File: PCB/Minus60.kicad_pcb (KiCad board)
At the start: 2 copper layers, 285.2 x 77.2 mm, 79 parts, among them P0 USB, SW0 SW_PUSH, SW0:0 SWITCH_DIODE, SW0:1 SWITCH_DIODE, SW0:10 SWITCH_DIODE, SW0:11 SWITCH_DIODE, SW0:12 SWITCH_DIODE, SW0:13 SWITCH_DIODE, SW0:2 SWITCH_DIODE, SW0:3 SWITCH_DIODE, SW0:4 SWITCH_DIODE, SW0:5 SWITCH_DIODE, SW0:6 SWITCH_DIODE, SW0:7 SWITCH_DIODE, SW0:8 SWITCH_DIODE, SW0:9 SWITCH_DIODE, SW1:0 SWITCH_DIODE, SW1:1 SWITCH_DIODE, SW1:10 SWITCH_DIODE, SW1:11 SWITCH_DIODE, SW1:13 SWITCH_DIODE, SW1:2 SWITCH_DIODE, SW1:3 SWITCH_DIODE, SW1:4 SWITCH_DIODE, SW1:5 SWITCH_DIODE, SW1:6 SWITCH_DIODE, SW1:7 SWITCH_DIODE, SW1:8 SWITCH_DIODE, SW1:9 SWITCH_DIODE, SW2:0 SWITCH_DIODE, SW2:10 SWITCH_DIODE, SW2:11 SWITCH_DIODE, SW2:13 SWITCH_DIODE, SW2:2 SWITCH_DIODE, SW2:3 SWITCH_DIODE, SW2:4 SWITCH_DIODE, SW2:5 SWITCH_DIODE, SW2:6 SWITCH_DIODE, SW2:7 SWITCH_DIODE, SW2:8 SWITCH_DIODE, SW2:9 SWITCH_DIODE, SW3:0 SWITCH_DIODE, SW3:1 SWITCH_DIODE, SW3:10 SWITCH_DIODE, SW3:11 SWITCH_DIODE, SW3:12 SWITCH_DIODE, SW3:13 SWITCH_DIODE, SW3:3 SWITCH_DIODE, SW3:6 SWITCH_DIODE

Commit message: Add stabilizers
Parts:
- added ?: , Keyboards:VIA-0.6, F.Cu at (138.2, 94.0)
- UW0: value USBWireConnection -> (none)
- moved ? 90.3 mm to (266.2, 33.0)
- moved ? 44.4 mm to (180.1, 89.4)
- moved ? 41.2 mm to (120.1, 91.7)
- moved PM0 15.8 mm to (168.1, 93.0)
- moved ? 14.7 mm to (136.9, 101.6)
- moved ? 14.3 mm to (149.9, 100.1)
- moved ? 12.3 mm to (161.0, 73.7)
- moved SW0 8.87 mm to (98.6, 98.6), turned to 180 degrees
- moved ? 3.18 mm to (144.8, 87.1)
- moved UW0 1.61 mm to (148.3, 86.4), turned to 45 degrees
- moved ? 1.27 mm to (137.2, 93.5), turned to 0 degrees
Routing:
- net /COL13: track 155.3 -> 181.4 mm, vias 1 -> 0
- net /COL9: track 68.1 -> 88.5 mm
- net /COL12: track 127.6 -> 144.4 mm
- net /COL6: track 136.0 -> 119.2 mm
- net /COL10: track 112.0 -> 127.6 mm, vias 0 -> 1
- net /COL4: track 162.8 -> 147.8 mm
- net /COL11: track 120.8 -> 135.2 mm
- net /COL7: track 83.3 -> 70.0 mm, vias 2 -> 0
- net /COL3: track 199.6 -> 186.8 mm, vias 1 -> 2
- net /COL5: track 143.5 -> 131.5 mm, vias 2 -> 0
- net /COL1: track 216.0 -> 204.1 mm, vias 3 -> 1
- net /RST: track 81.3 -> 71.1 mm
- net /COL0: track 234.3 -> 226.4 mm, vias 3 -> 1
- net /ROW3: track 286.2 -> 289.7 mm
- net /COL2: track 194.7 -> 197.0 mm, vias 3 -> 2
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
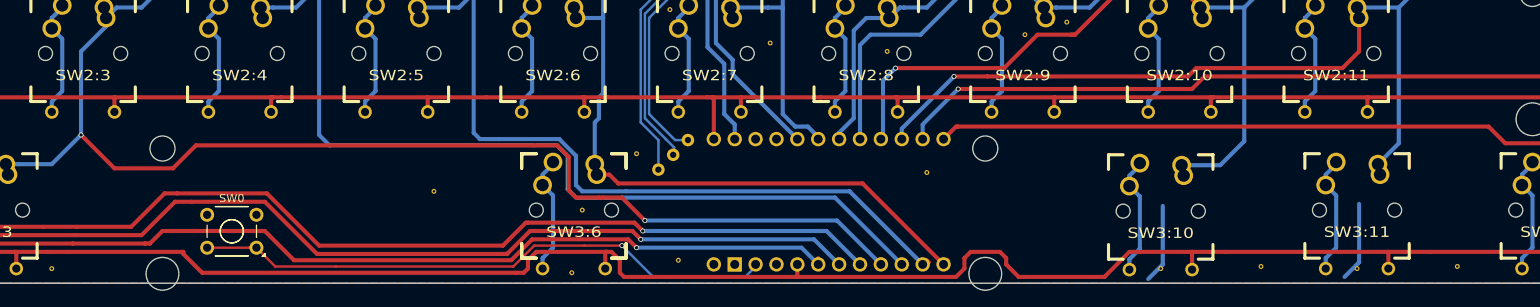
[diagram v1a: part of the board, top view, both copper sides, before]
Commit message: Flip spacebar stabilizer
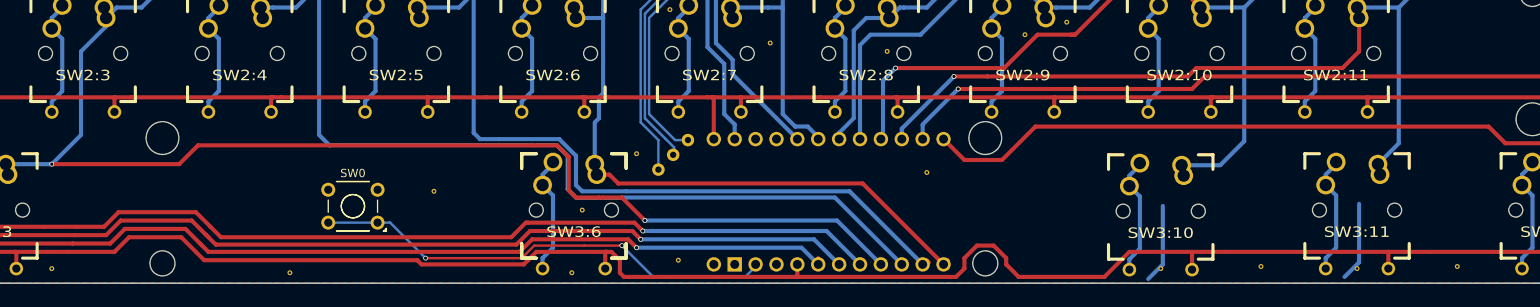
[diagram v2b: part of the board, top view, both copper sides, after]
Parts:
- added ?: , Keyboards:VIA-0.6, F.Cu at (102.6, 101.6)
- moved SW0 15.0 mm to (113.3, 95.5)
- turned ? to 180 degrees
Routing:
- net /RST: track 71.1 -> 56.8 mm, vias 1 -> 2
- net /COL1: track 204.1 -> 201.2 mm
- net /COL2: track 197.0 -> 194.3 mm
- net /COL13: track 181.4 -> 183.5 mm
- net /COL3: track 186.8 -> 188.4 mm
- net /COL0: track 226.4 -> 225.8 mm
- net /ROW3: track 289.7 -> 290.3 mm

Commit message: Add logo
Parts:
- turned ? to 0 degrees
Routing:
- net (no net): track 19.5 -> 0.00 mm
- net /COL13: track 183.5 -> 182.5 mm
- net /COL3: track 188.4 -> 189.3 mm
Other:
- board text added: "-60°"
- board text added: "Minus60"

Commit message: Add actual cherry support
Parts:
- added ?: , Keyboards:VIA-0.6, F.Cu at (114.0, -9.91)
- added ?: , Keyboards:VIA-0.6, F.Cu at (130.6, -77.2)
- UW0: value (none) -> USBWireConnection
- moved ? 122.4 mm to (136.1, -20.8)
- moved ? 116.8 mm to (131.6, -22.6)
- moved ? 116.7 mm to (137.2, -9.91)
- moved ? 113.3 mm to (164.8, -39.6)
- moved ? 112.8 mm to (191.3, -40.1)
- moved ? 111.0 mm to (280.2, -9.65)
- moved ? 111.0 mm to (256.3, -9.65)
- moved ? 111.0 mm to (208.5, -9.91)
- moved ? 111.0 mm to (232.4, -9.91)
- moved ? 111.0 mm to (120.1, -19.3)
- moved ? 111.0 mm to (180.1, -21.6)
- moved ? 111.0 mm to (73.7, -9.91)
- moved ? 111.0 mm to (30.5, -9.91)
- moved ? 111.0 mm to (65.5, -9.91)
- moved ? 111.0 mm to (42.2, -9.91)
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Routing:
- net /COL4: track 147.8 -> 152.6 mm
- net /COL3: track 189.3 -> 193.6 mm
- net /ROW0: track 365.8 -> 368.8 mm, vias 1 -> 3
- net /ROW3: track 290.3 -> 287.4 mm
- net /COL12: track 144.4 -> 142.1 mm
- net /COL6: track 119.2 -> 121.3 mm
- net /COL5: track 131.5 -> 129.6 mm
- net /COL9: track 88.5 -> 86.8 mm
- net /RST: track 56.8 -> 55.5 mm
- net /COL8: track 67.5 -> 66.4 mm
- net /COL1: track 201.2 -> 200.4 mm
- net /ROW1: track 300.3 -> 301.1 mm
- net /COL11: track 135.2 -> 136.0 mm
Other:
- board size 285.2 x 77.2 mm -> 285.2 x 79 mm
- board text added: "D+"
- board text added: "D-"
- board text added: "VCC"

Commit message: Fix random issues
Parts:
- added ?: , Keyboards:VIA-0.6, F.Cu at (172.7, -32.5)
- moved UW0 1.27 mm to (148.3, -25.9)
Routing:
- net /COL0: track 226.2 -> 228.0 mm
- net /COL10: track 127.7 -> 125.9 mm
- net /COL11: track 136.0 -> 137.3 mm
- net Net-(P0-Pad3): track 61.0 -> 59.7 mm
- net Net-(P0-Pad2): track 63.0 -> 61.7 mm
- net /COL8: track 66.4 -> 67.3 mm
- net Net-(P0-Pad1): track 59.6 -> 59.1 mm
